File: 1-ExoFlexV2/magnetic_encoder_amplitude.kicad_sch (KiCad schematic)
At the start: 56 parts, among them J59 Tulip Conn, J60 Tulip Conn, J61 Tulip Conn, J62 Tulip Conn, J63 Tulip Conn, J64 Tulip Conn, J65 Jumper, J66 Jumper, J67 Jumper, J68 Jumper, J69 Jumper, J70 Jumper, J71 Jumper, J72 Jumper, J73 Jumper, U20 COMP, U21 COMP, U22 COMP, U23 OR Gate, U24 OR Gate

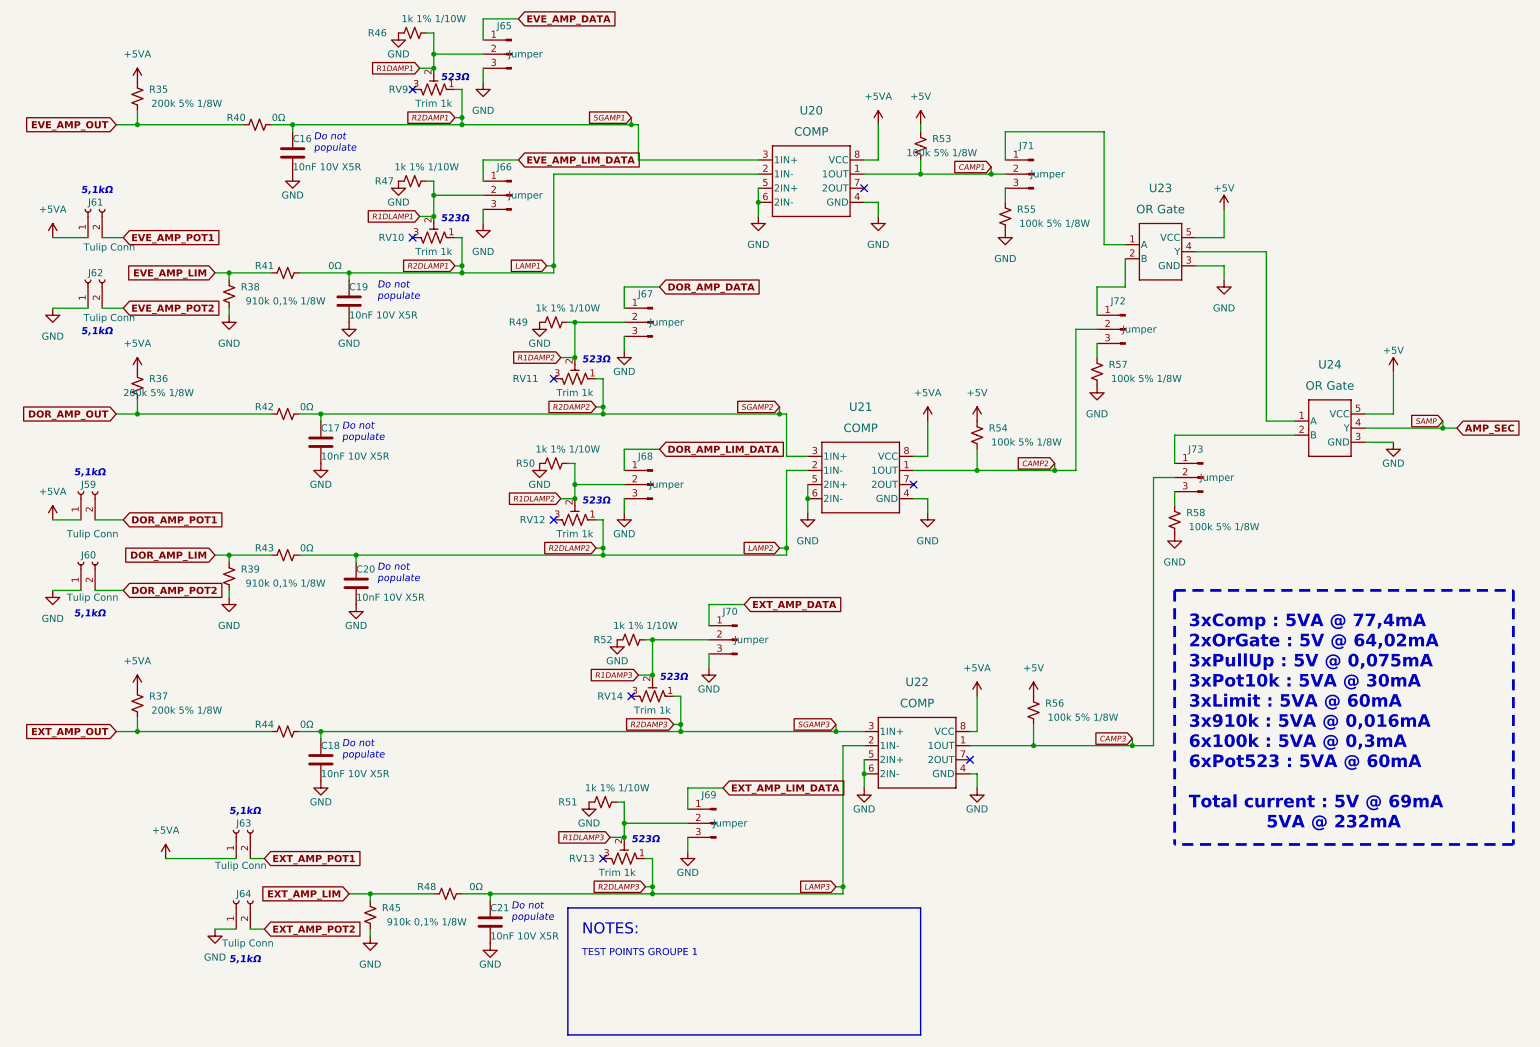
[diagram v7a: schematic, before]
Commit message: Finalisation 3
- Changement des régulateur de tension
- Retrait de test point inutile
- Changement de jumper mal positionner
- Ajout de Mounting holes et fiducial
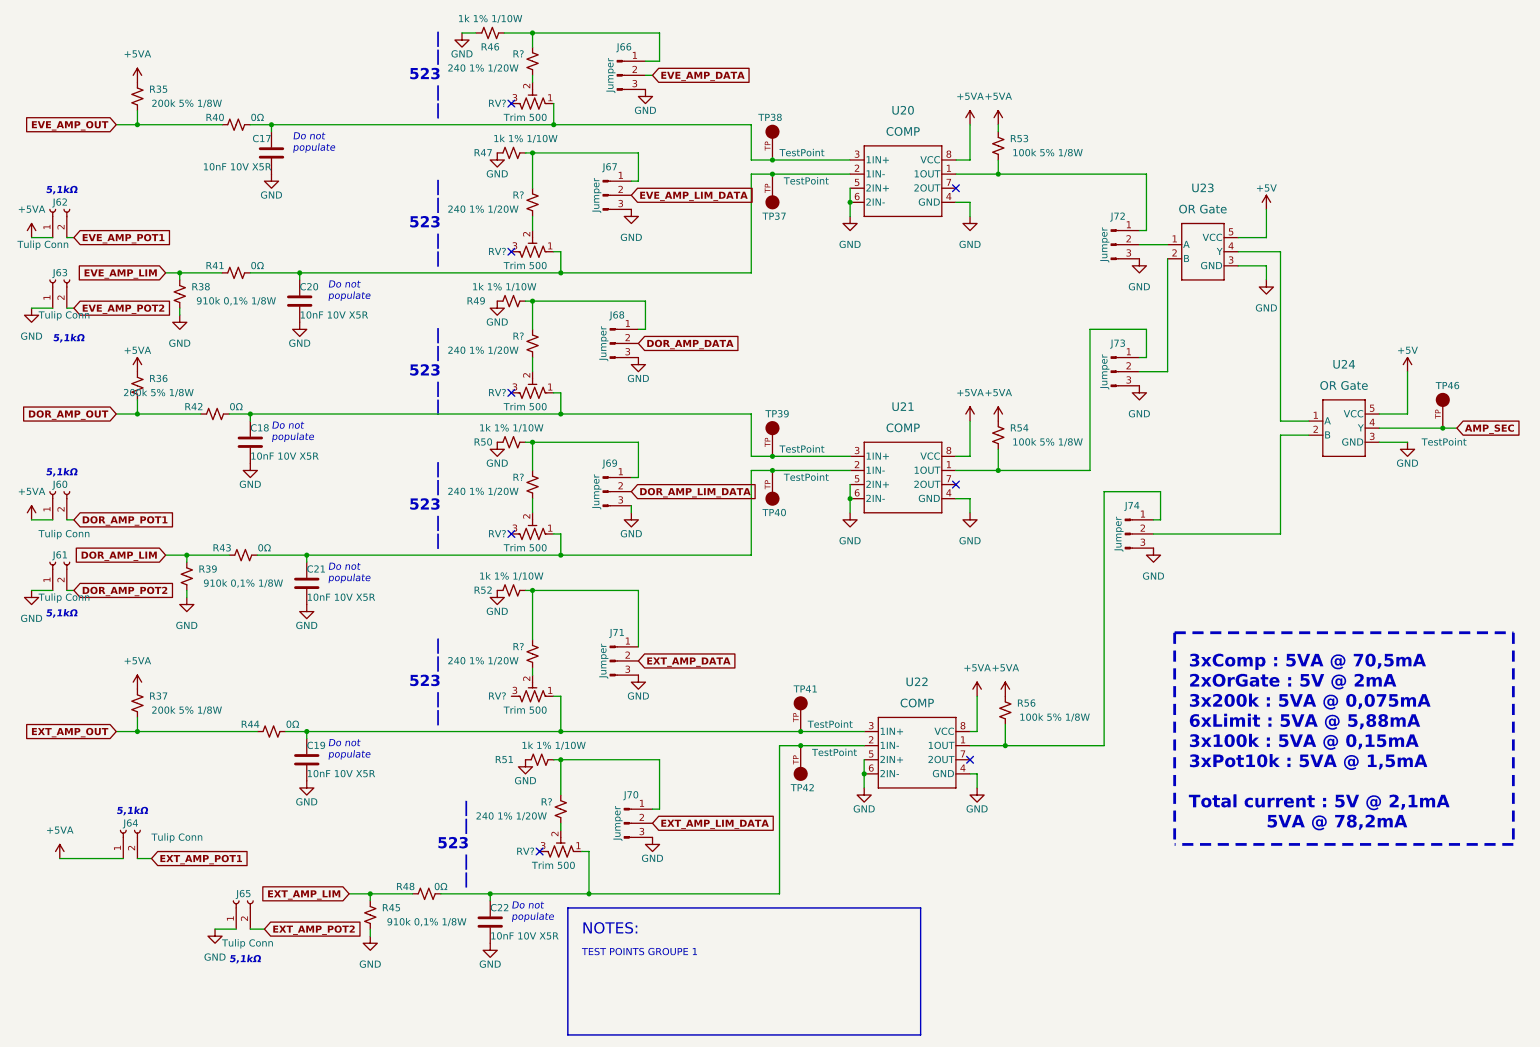
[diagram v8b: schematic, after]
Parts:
- removed C16: 10nF 10V X5R, Capacitor_SMD:C_01005_0402Metric, symbol Device:C
- removed R55, R57, R58: 100k 5% 1/8W, Resistor_SMD:R_0805_2012Metric, symbol Device:R_Small_US
- removed RV10, RV11, RV12, RV13, RV14, RV9: Trim 1k, FootPrint:TRIM_3362P-1-102LF, symbol Device:R_Potentiometer_Trim_US
- added C22: 10nF 10V X5R, Capacitor_SMD:C_0603_1608Metric, symbol Device:C
- added R? (x6): 240 1% 1/20W, Resistor_SMD:R_0201_0603Metric, symbol Device:R_Small_US
- added RV? (x6): Trim 500, FootPrint:TRIM_3296W-1-501LF, symbol Device:R_Potentiometer_Trim_US
- added TP37, TP38, TP39, TP40, TP41, TP42, TP46: TestPoint, FootPrint:KEYSTONE_5005, symbol SymLib:5005
- C17, C18, C19, C20, C21: footprint Capacitor_SMD:C_01005_0402Metric -> Capacitor_SMD:C_0603_1608Metric; DESCRIPTION 10000 pF ±10% 10V Ceramic Capacitor X5R 01005 (0402 Metric) -> 10000 pF ±5% 10V Ceramic Capacitor U2J 0603 (1608 Metric); PACKAGE 01005 (0402 Metric) -> 0603 (1608 Metric); PART NUMBER GRM022R61A103KE19L -> GRM1857U1A103JA44D
- J66: renamed from J65; footprint Connector_PinSocket_2.54mm:PinSocket_1x03_P2.54mm_Vertical -> Connector_PinHeader_2.54mm:PinHeader_1x03_P2.54mm_Vertical
- J67: renamed from J66; footprint Connector_PinSocket_2.54mm:PinSocket_1x03_P2.54mm_Vertical -> Connector_PinHeader_2.54mm:PinHeader_1x03_P2.54mm_Vertical
- J68: renamed from J67; footprint Connector_PinSocket_2.54mm:PinSocket_1x03_P2.54mm_Vertical -> Connector_PinHeader_2.54mm:PinHeader_1x03_P2.54mm_Vertical
- J69: renamed from J68; footprint Connector_PinSocket_2.54mm:PinSocket_1x03_P2.54mm_Vertical -> Connector_PinHeader_2.54mm:PinHeader_1x03_P2.54mm_Vertical
- J70: renamed from J69; footprint Connector_PinSocket_2.54mm:PinSocket_1x03_P2.54mm_Vertical -> Connector_PinHeader_2.54mm:PinHeader_1x03_P2.54mm_Vertical
- J71: renamed from J70; footprint Connector_PinSocket_2.54mm:PinSocket_1x03_P2.54mm_Vertical -> Connector_PinHeader_2.54mm:PinHeader_1x03_P2.54mm_Vertical
- J72: renamed from J71; footprint Connector_PinSocket_2.54mm:PinSocket_1x03_P2.54mm_Vertical -> Connector_PinHeader_2.54mm:PinHeader_1x03_P2.54mm_Vertical
- J73: renamed from J72; footprint Connector_PinSocket_2.54mm:PinSocket_1x03_P2.54mm_Vertical -> Connector_PinHeader_2.54mm:PinHeader_1x03_P2.54mm_Vertical
- J74: renamed from J73; footprint Connector_PinSocket_2.54mm:PinSocket_1x03_P2.54mm_Vertical -> Connector_PinHeader_2.54mm:PinHeader_1x03_P2.54mm_Vertical
- renumbered J59 to J60, J60 to J61, J61 to J62, J62 to J63, J63 to J64, J64 to J65
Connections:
- net +5V: no longer R53.1, R54.1, R56.1
- net +5VA: now also R53.1, R54.1, R56.1
- net AMP_SEC: now also TP46.TP
- net DOR_AMP_DATA: now also J68.2 (Pin_2); no longer J68.1 (Pin_1)
- net DOR_AMP_LIM_DATA: now also J69.2 (Pin_2); no longer J69.1 (Pin_1)
- net EVE_AMP_DATA: now also J66.2 (Pin_2); no longer J66.1 (Pin_1)
- net EVE_AMP_LIM_DATA: now also J67.2 (Pin_2); no longer J67.1 (Pin_1)
- net EXT_AMP_DATA: now also J71.2 (Pin_2); no longer J71.1 (Pin_1)
- net EXT_AMP_LIM_DATA: now also J70.2 (Pin_2); no longer J70.1 (Pin_1)
- net GND: now also J72.3 (Pin_3), J73.3 (Pin_3), J74.3 (Pin_3), C22.2
- net at U24.2 (B): now also J74.2 (Pin_2); no longer J74.1 (Pin_1)
- net at J72.1 (Pin_1): now also R53.2, U20.1 (1OUT); no longer U23.1 (A)
- net at U23.2 (B): now also J73.2 (Pin_2); no longer J73.1 (Pin_1)
- removed net CAMP1: J72.2 (Pin_2), R53.2, U20.1 (1OUT)
- net CAMP2: no longer names the net of R54.2, U21.1 (1OUT)
- net CAMP2: now also J73.1 (Pin_1); no longer J73.2 (Pin_2)
- net CAMP3: no longer names the net of R56.2, U22.1 (1OUT)
- net CAMP3: now also J74.1 (Pin_1); no longer J74.2 (Pin_2)
- net LAMP1: no longer names the net of R41.2, U20.2 (1IN-)
- net LAMP1: now also C20.1, RV?.1, TP37.TP; no longer C19.1
- net LAMP2: no longer names the net of R43.2, U21.2 (1IN-)
- net LAMP2: now also C21.1, RV?.1, TP40.TP; no longer C20.1
- net LAMP3: no longer names the net of R48.2, U22.2 (1IN-)
- net LAMP3: now also C22.1, RV?.1, TP42.TP; no longer C21.1
- net R1DAMP1: no longer names the net of R46.2
- net R1DAMP1: now also J66.1 (Pin_1), R?.2; no longer J66.2 (Pin_2)
- net R1DAMP2: no longer names the net of R49.2
- net R1DAMP2: now also J68.1 (Pin_1), R?.2; no longer J68.2 (Pin_2)
- net R1DAMP3: no longer names the net of R52.2
- net R1DAMP3: now also J71.1 (Pin_1), R?.2; no longer J71.2 (Pin_2)
- net R1DLAMP1: no longer names the net of R47.2
- net R1DLAMP1: now also J67.1 (Pin_1), R?.2; no longer J67.2 (Pin_2)
- net R1DLAMP2: no longer names the net of R50.2
- net R1DLAMP2: now also J69.1 (Pin_1), R?.2; no longer J69.2 (Pin_2)
- net R1DLAMP3: no longer names the net of R51.2
- net R1DLAMP3: now also J70.1 (Pin_1), R?.2; no longer J70.2 (Pin_2)
- net R2DAMP1: no longer names the net of R40.2, U20.3 (1IN+)
- net R2DAMP1: now also C17.1, RV?.1, TP38.TP
- net R2DAMP2: no longer names the net of R42.2, U21.3 (1IN+)
- net R2DAMP2: now also C18.1, RV?.1, TP39.TP; no longer C17.1
- net R2DAMP3: no longer names the net of R44.2, U22.3 (1IN+)
- net R2DAMP3: now also C19.1, RV?.1, TP41.TP; no longer C18.1
- new net: R?.1, RV?.2 (x6)
- new net: J72.2 (Pin_2), U23.1 (A)
- no-connect marks 9 -> 8
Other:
- note added: "3xComp : 5VA @ 70,5mA 2xOrGate : 5V @ 2mA 3x200k : 5VA @ 0,075mA 6xLimit : 5VA @ 5,88mA 3x100k : 5VA @ 0,15mA 3xPot10k : 5VA @ 1,5mA Total current : 5V @ 2,1mA 5VA @ 78,2mA"
- note added: "| | 523 | |"
- note removed: "3xComp : 5VA @ 77,4mA 2xOrGate : 5V @ 64,02mA 3xPullUp : 5V @ 0,075mA 3xPot10k : 5VA @ 30mA 3xLimit : 5VA @ 60mA 3x910k : 5VA @ 0,016mA 6x100k : 5VA @ 0,3mA 6xPot523 : 5VA @ 60mA Total current : 5V @ 69mA 5VA @ 232mA"
- note removed: "523Ω"
- moved on the sheet: J60, J61, J62, J63, J64, J66, J67, J68, J69, J70, J71, J72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
